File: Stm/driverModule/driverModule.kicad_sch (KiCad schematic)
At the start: 6 parts, among them U101 STM32G431KBTx, U102 ADM7171ACPZ-3.0-R7, U103 TJA1051T-3

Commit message: Add Headers
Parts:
- added C104: 10nF, symbol Device:C
- added C105: 470uF, symbol Device:C_Polarized
- added C106: 4u7F, symbol Device:C
- added D101: B340, Diode_SMD:D_SMC, symbol Diode:B340
- added L101: 22uH, symbol Device:L
- added R101, R102: R_US, symbol Device:R_US
- added U104: TPS5410DR, Package_SO:SOIC-8-N7_3.9x4.9mm_P1.27mm, symbol Local_symbols:TPS5410DR
- added U105: SN74LV165APWR, Package_SO:TSSOP-16_4.4x5mm_P0.65mm, symbol Local_symbols:SN74LV165APWR
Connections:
- net +3V3: now also U105.16 (VCC)
- net +5V: now also C105.1, L101.2, R101.1
- net GND: now also C105.2, C106.1, D101.2 (A), R102.2, U104.6 (GND), U105.8 (GND)
- net SpiClock: now reaches U101.10 (PA5)
- net SpiClock: now also U105.2 (CLK)
- net SpiMasterInput: now reaches U101.11 (PA6)
- net SpiMasterInput: now also U105.9 (QH)
- net SpiMasterOutput: now reaches U101.12 (PA7)
- net ParallelLoad: now reaches U101.18 (PA8)
- net ParallelLoad: now also U105.1 (SH/~LD)
- net Inhibit: now reaches U101.19 (PA9)
- net Inhibit: now also U105.15 (CLK_INH)
- new net: C104.1, U104.1 (BOOT)
- new net: R101.2, R102.1, U104.4 (VSENSE)
- new net: C104.2, D101.1 (K), L101.1, U104.8 (PH)
- new net +12V: C106.2, U104.5 (ENA), U104.7 (VIN)
- no-connect marks 0 -> 4
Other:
- moved on the sheet: C101, C102, C103, U101, U102

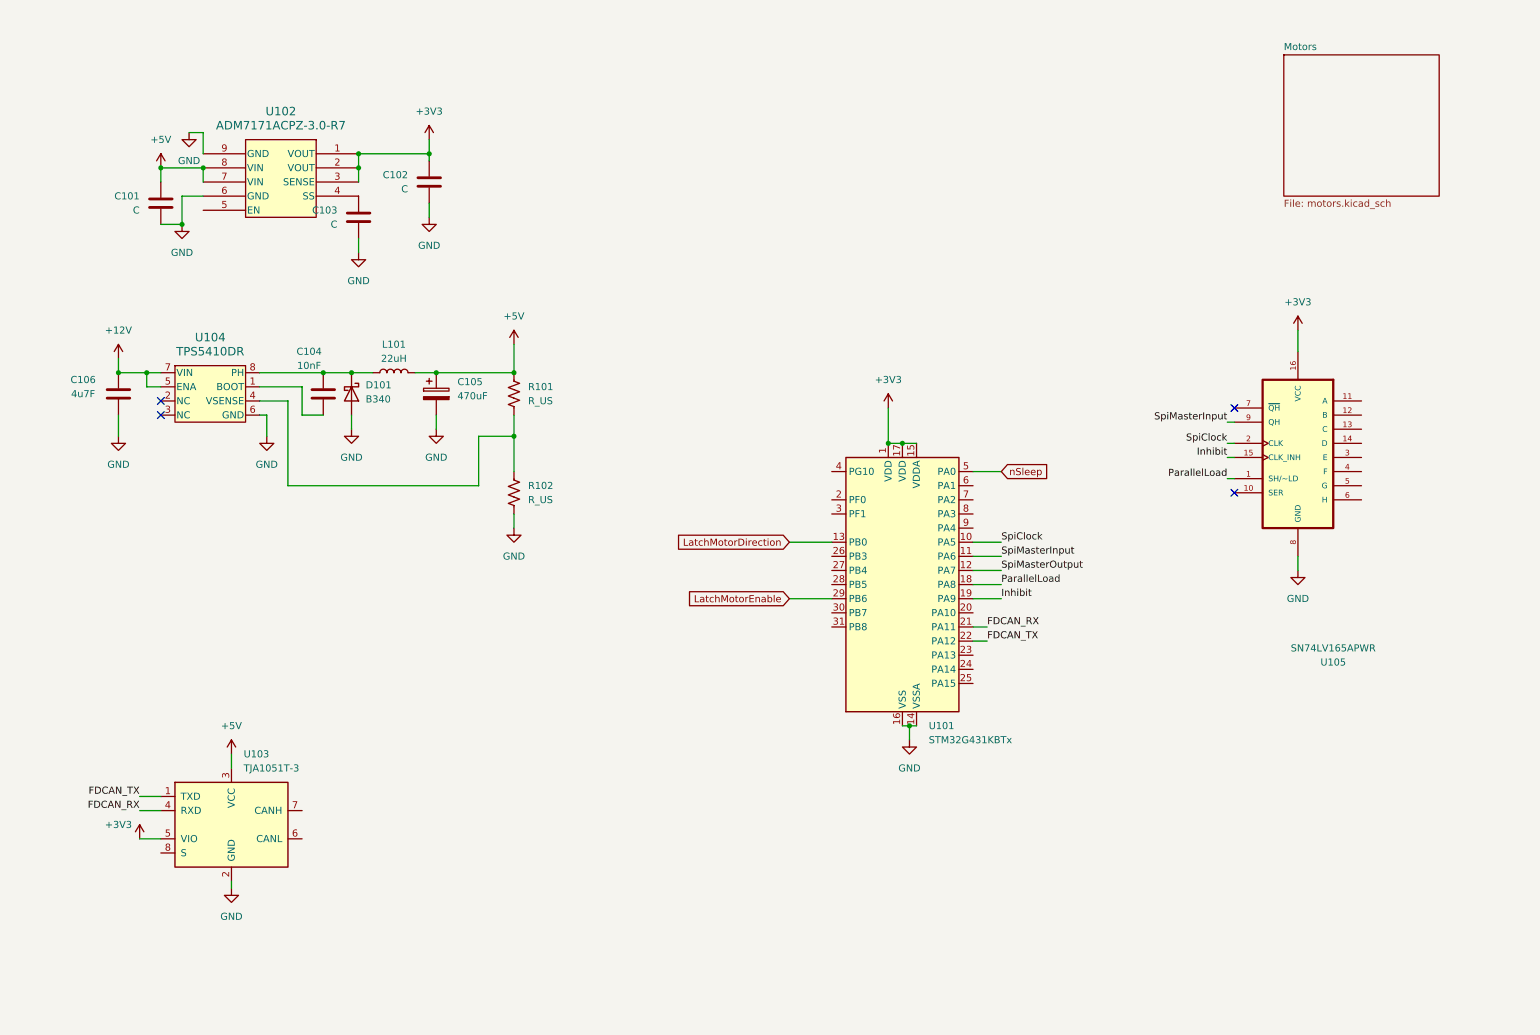
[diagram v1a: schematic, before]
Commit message: CD40109BNSR
Added low to high level shifter
and foot print
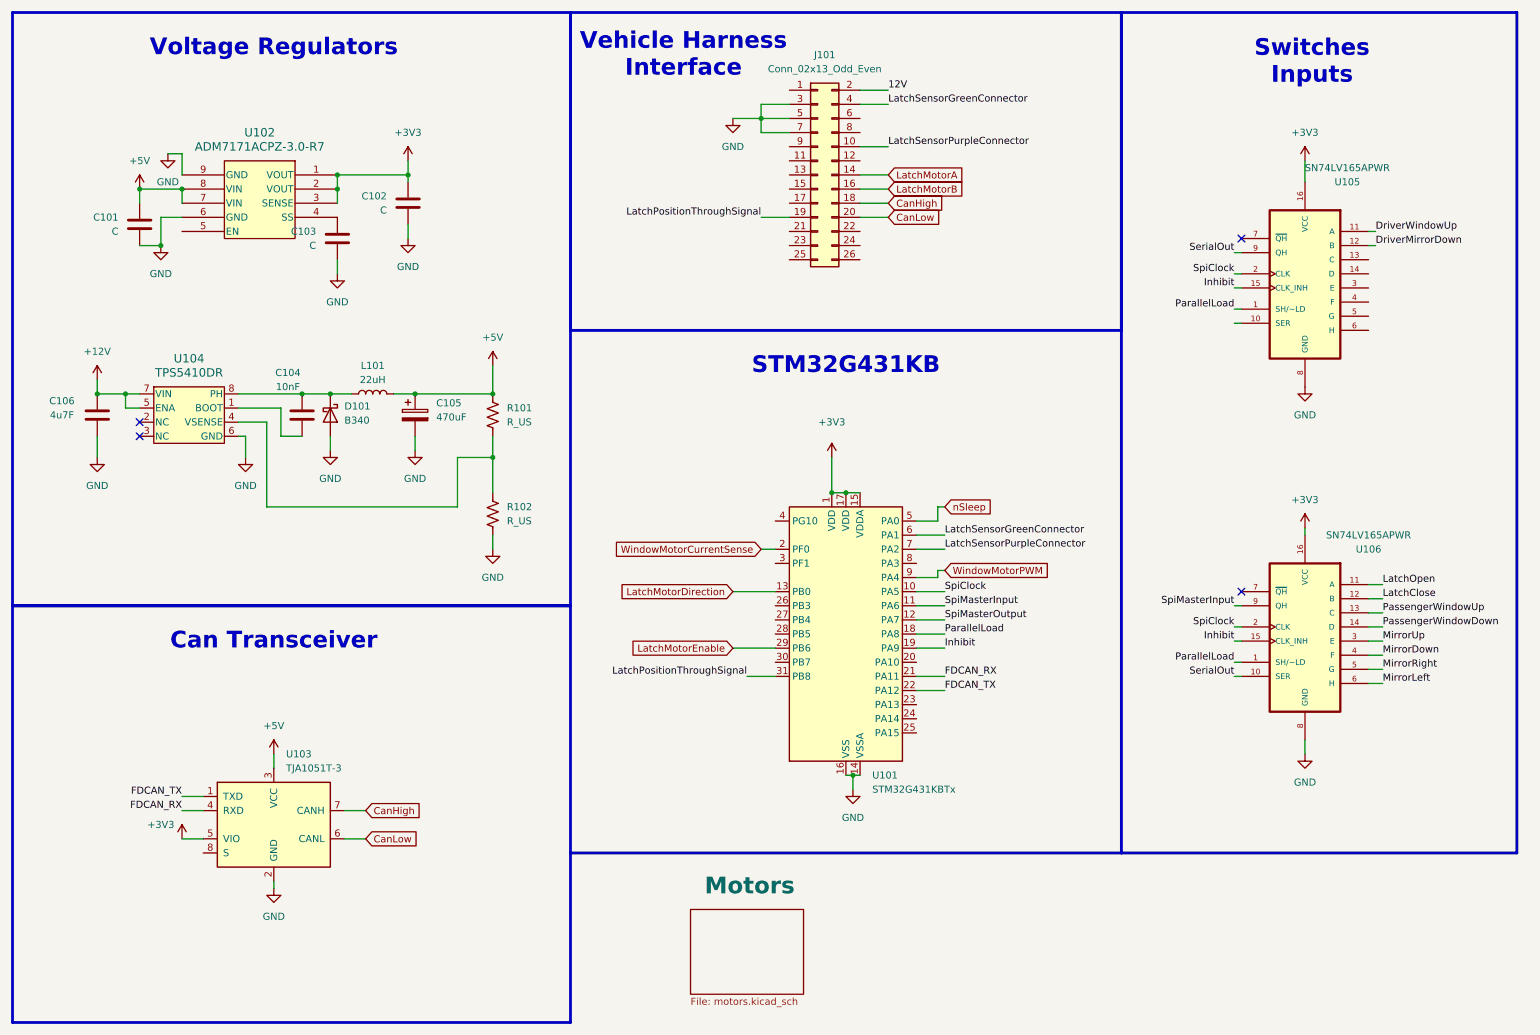
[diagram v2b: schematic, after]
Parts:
- added J101: Conn_02x13_Odd_Even, symbol Connector_Generic:Conn_02x13_Odd_Even
- added U106: SN74LV165APWR, Package_SO:TSSOP-16_4.4x5mm_P0.65mm, symbol Local_symbols:SN74LV165APWR
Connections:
- net +3V3: now also U106.16 (VCC)
- net GND: now also J101.3 (Pin_3), J101.5 (Pin_5), J101.7 (Pin_7), U106.8 (GND)
- net Inhibit: now also U106.15 (CLK_INH)
- net ParallelLoad: now also U106.1 (SH/~LD)
- net SpiClock: now also U106.2 (CLK)
- net SpiMasterInput: now also U106.9 (QH); no longer U105.9 (QH)
- net CanLow: now reaches U103.6 (CANL)
- net CanLow: now also J101.20 (Pin_20)
- net CanHigh: now reaches U103.7 (CANH)
- net CanHigh: now also J101.18 (Pin_18)
- net WindowMotorCurrentSense: now reaches U101.2 (PF0)
- net LatchPositionThroughSignal: now reaches U101.31 (PB8)
- net LatchPositionThroughSignal: now also J101.19 (Pin_19)
- net LatchSensorGreenConnector: now reaches U101.6 (PA1)
- net LatchSensorGreenConnector: now also J101.4 (Pin_4)
- net LatchSensorPurpleConnector: now reaches U101.7 (PA2)
- net LatchSensorPurpleConnector: now also J101.10 (Pin_10)
- net WindowMotorPWM: now reaches U101.9 (PA4)
- net DriverWindowUp: now reaches U105.11 (A)
- net DriverMirrorDown: now reaches U105.12 (B)
- new net 12V: J101.2 (Pin_2)
- new net LatchClose: U106.12 (B)
- new net LatchMotorA: J101.14 (Pin_14)
- new net LatchMotorB: J101.16 (Pin_16)
- new net LatchOpen: U106.11 (A)
- new net MirrorDown: U106.4 (F)
- new net MirrorLeft: U106.6 (H)
- new net MirrorRight: U106.5 (G)
- new net MirrorUp: U106.3 (E)
- new net PassengerWindowDown: U106.14 (D)
- new net PassengerWindowUp: U106.13 (C)
- new net SerialOut: U105.9 (QH), U106.10 (SER)
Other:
- note added: "Can Transceiver"
- note added: "STM32G431KB"
- note added: "Switches Inputs"
- note added: "Vehicle Harness Interface"
- note added: "Voltage Regulators"
- moved on the sheet: C101, C102, C103, C104, C105, C106, D101, L101, R101, R102, U101, U102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

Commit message: Mirror Motors and key fob
Changed for a 3 half bridge semiconductor
Added level shift translator for key fob input
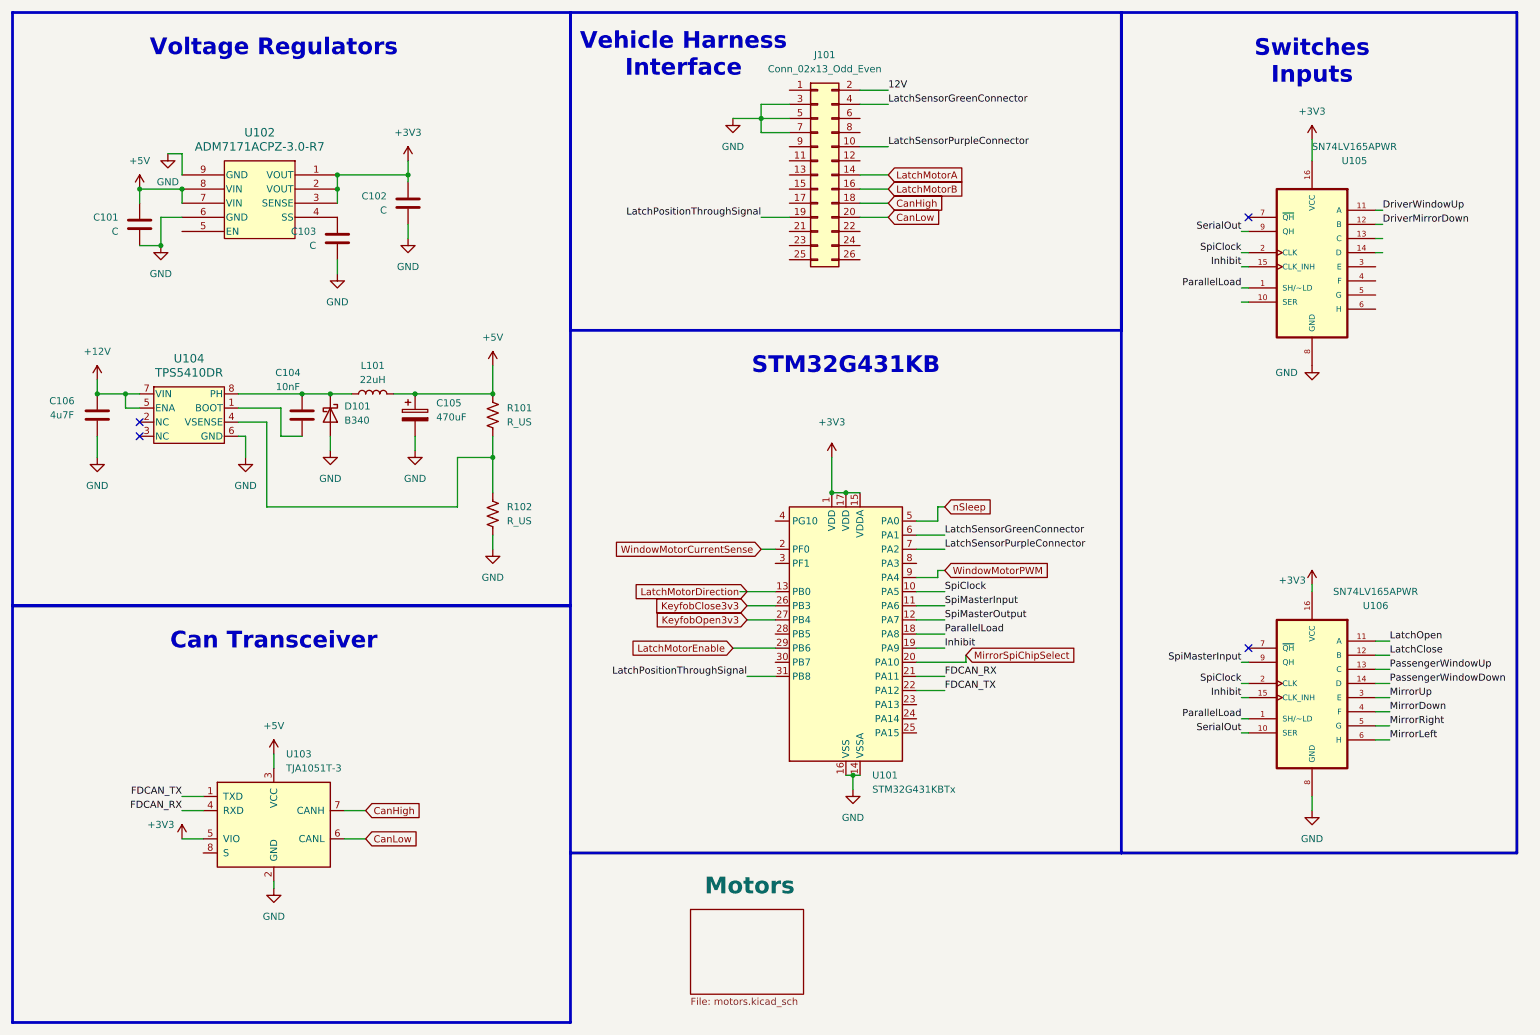
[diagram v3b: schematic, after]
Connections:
- net MirrorSpiChipSelect: now reaches U101.20 (PA10)
- net KeyfobClose3v3: now reaches U101.26 (PB3)
- net KeyfobOpen3v3: now reaches U101.27 (PB4)
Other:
- moved on the sheet: U105, U106

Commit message: Connector
Removed processor and add a two SMD connectors to plug a MCU carrier board
Generate first Printed Circuit board layout
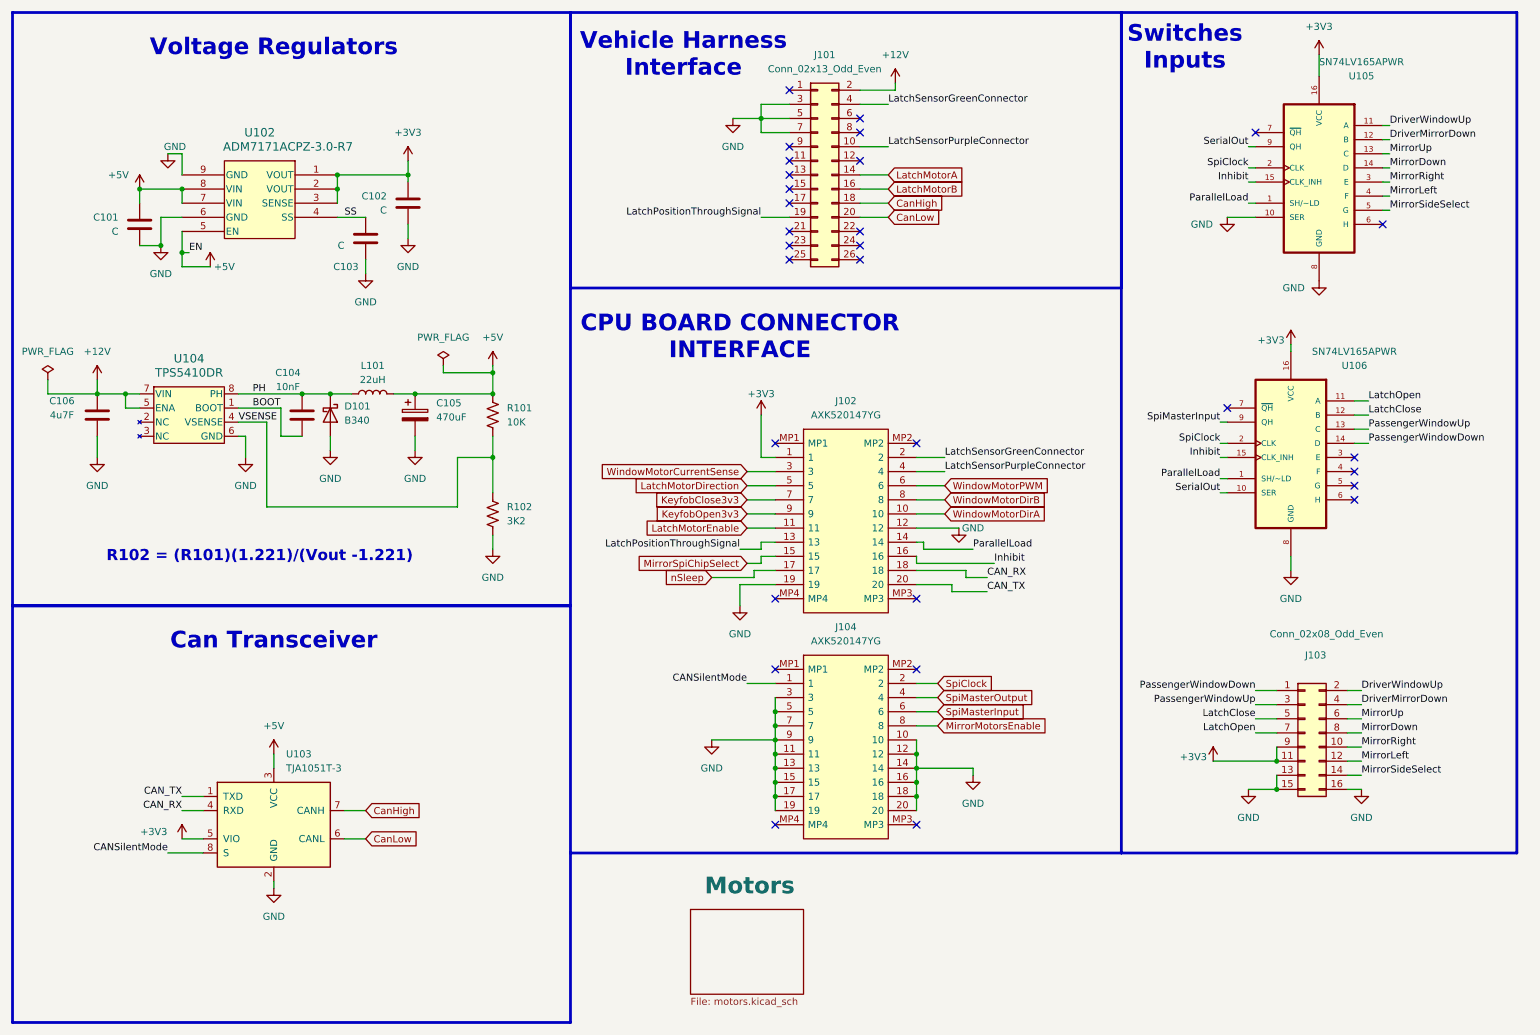
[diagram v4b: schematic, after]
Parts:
- removed U101: STM32G431KBTx, Package_QFP:LQFP-32_7x7mm_P0.8mm, symbol MCU_ST_STM32G4:STM32G431KBTx
- added J102, J104: AXK520147YG, Local_Footprints:AXK520147YG, symbol _Connectors:AXK520147YG
- added J103: Conn_02x08_Odd_Even, Connector_PinHeader_2.54mm:PinHeader_2x08_P2.54mm_Vertical, symbol Connector_Generic:Conn_02x08_Odd_Even
- C101, C102, C103: footprint (none) -> Capacitor_SMD:C_0402_1005Metric_Pad0.74x0.62mm_HandSolder
- C104, C106: footprint (none) -> Capacitor_SMD:C_0805_2012Metric
- C105: footprint (none) -> Capacitor_SMD:CP_Elec_10x10
- J101: footprint (none) -> Connector_PinHeader_2.54mm:PinHeader_2x13_P2.54mm_Vertical
- L101: footprint (none) -> Local_Footprints:L-SMD-13.45x12.6X5.0mm
- R101: value R_US -> 10K; footprint (none) -> Resistor_SMD:R_0402_1005Metric_Pad0.72x0.64mm_HandSolder
- R102: value R_US -> 3K2; footprint (none) -> Resistor_SMD:R_0402_1005Metric_Pad0.72x0.64mm_HandSolder
- U104: footprint Package_SO:SOIC-8-N7_3.9x4.9mm_P1.27mm -> Local_Footprints:SOIC-8-1EP_3.9x4.9mm_P1.27mm
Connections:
- net 12V is gone; now on net +12V: J101.2 (Pin_2)
- net +3V3: now also J102.1, J103.11 (Pin_11), J103.9 (Pin_9)
- net +5V: now also U102.5 (EN)
- net DriverMirrorDown: now also J103.4 (Pin_4)
- net DriverWindowUp: now also J103.2 (Pin_2)
- net GND: now also U105.10 (SER), J102.12, J102.19, J103.13 (Pin_13), J103.15 (Pin_15), J103.16 (Pin_16), J104.10, J104.11, J104.12, J104.13, J104.14, J104.15, J104.16, J104.17, J104.18, J104.19, J104.20, J104.3, J104.5, J104.7, J104.9
- net Inhibit: now also J102.16
- net KeyfobClose3v3: now also J102.7
- net KeyfobOpen3v3: now also J102.9
- net LatchClose: now also J103.5 (Pin_5)
- net LatchMotorDirection: now also J102.5
- net LatchMotorEnable: now also J102.11
- net LatchOpen: now also J103.7 (Pin_7)
- net LatchPositionThroughSignal: now also J102.13
- net LatchSensorGreenConnector: now also J102.2
- net LatchSensorPurpleConnector: now also J102.4
- net MirrorDown: now also U105.14 (D), J103.8 (Pin_8); no longer U106.4 (F)
- net MirrorLeft: now also U105.4 (F), J103.12 (Pin_12); no longer U106.6 (H)
- net MirrorRight: now also U105.3 (E), J103.10 (Pin_10); no longer U106.5 (G)
- net MirrorSpiChipSelect: now also J102.15
- net MirrorUp: now also U105.13 (C), J103.6 (Pin_6); no longer U106.3 (E)
- net ParallelLoad: now also J102.14
- net PassengerWindowDown: now also J103.1 (Pin_1)
- net PassengerWindowUp: now also J103.3 (Pin_3)
- net SpiClock: now also J104.2
- net SpiMasterInput: now also J104.6
- net SpiMasterOutput: now also J104.4
- net WindowMotorCurrentSense: now also J102.3
- net WindowMotorPWM: now also J102.6
- net nSleep: now also J102.17
- net BOOT: now reaches C104.1, U104.1 (BOOT)
- net VSENSE: now reaches R101.2, R102.1, U104.4 (VSENSE)
- net PH: now reaches C104.2, D101.1 (K), L101.1, U104.8 (PH)
- net CANSilentMode: now reaches U103.8 (S)
- net CANSilentMode: now also J104.1
- net SS: now reaches C103.1, U102.4 (SS)
- net MirrorSideSelect: now reaches U105.5 (G)
- net MirrorSideSelect: now also J103.14 (Pin_14)
- net FDCAN_RX renamed CAN_RX
- net CAN_RX: now also J102.18
- net FDCAN_TX renamed CAN_TX
- net CAN_TX: now also J102.20
- new net MirrorMotorsEnable: J104.8
- new net WindowMotorDirA: J102.10
- new net WindowMotorDirB: J102.8
- no-connect marks 4 -> 30
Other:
- note added: "CPU BOARD CONNECTOR INTERFACE"
- note added: "R102 = (R101)(1.221)/(Vout -1.221)"
- note removed: "STM32G431KB"
- moved on the sheet: C103, U105, U106
